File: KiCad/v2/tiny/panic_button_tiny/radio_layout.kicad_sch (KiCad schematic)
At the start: 1 part

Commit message: [UPDATE] some of the pcb design and layout
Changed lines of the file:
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@@
 		(pin "1"
+		)
+		(pin "2"
 		)
 		(instances

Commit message: [UPDATE] some connections in the circuit
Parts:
- added C3: 1.2pF, Capacitor_SMD:C_01005_0402Metric_Pad0.57x0.30mm_HandSolder, symbol PCM_Elektuur:C
- added L1: 4.7nH, Capacitor_SMD:C_0402_1005Metric_Pad0.74x0.62mm_HandSolder, symbol PCM_Elektuur:L
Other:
- moved on the sheet: E1
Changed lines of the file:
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@@
+	)
+	(symbol
+		(lib_id "PCM_Elektuur:L")
+		(at 60.96 31.75 0)
+		(unit 1)
+		(body_style 1)
+		(exclude_from_sim no)
+		(in_bom yes)
+		(on_board yes)
+		(in_pos_files yes)
+		(dnp no)
+		(fields_autoplaced yes)
+		(property "Reference" "L1"
+			(at 63.5 30.4799 0)
+			(show_name no)
+			(do_not_autoplace no)
+			(effects
+				(font
+					(size 1.27 1.27)
+				)
+				(justify left)
+			)
+		)
+		(property "Value" "4.7nH"
+			(at 63.5 33.0199 0)
+			(show_name no)
+			(do_not_autoplace no)
+			(effects
+				(font
+					(size 1.27 1.27)
+				)
+				(justify left)
+			)
+		)
+		(property "Footprint" "Capacitor_SMD:C_0402_1005Metric_Pad0.74x0.62mm_HandSolder"
+			(at 60.96 31.75 0)
+			(hide yes)
+			(show_name no)
+			(do_not_autoplace no)
+			(effects
+				(font
+					(size 1.27 1.27)
+				)
+			)
+		)
+		(property "Datasheet" ""
+			(at 60.96 31.75 0)
+			(hide yes)
+			(show_name no)
+			(do_not_autoplace no)
+			(effects
+				(font
+					(size 1.27 1.27)
+				)
+			)
+		)
+		(property "Description" "coil/winding/inductor/choke/reactor"
+			(at 60.96 31.75 0)
+			(hide yes)
+			(show_name no)
+			(do_not_autoplace no)
+			(effects
+				(font
+					(size 1.27 1.27)
+				)
+			)
+		)
+		(property "Indicator" "●"
+			(at 60.833 29.21 0)
+			(hide yes)
+			(show_name no)
+			(do_not_autoplace no)
+			(effects
+				(font
+					(size 0.635 0.635)
+				)
+			)
+		)
+		(property "Rating" "A"
+			(at 59.69 34.925 0)
+			(hide yes)
+			(show_name no)
+			(do_not_autoplace no)
+			(effects
+				(font
+					(size 1.27 1.27)
+				)
+				(justify right)
+			)
+		)
+		(pin "1"
+		)
+		(pin "2"
+		)
+		(instances
+			(project "panic_button_tiny"
+				(path "/c4eb92e9-b42f-4db0-b1d9-0ef70f7ca601/87783f59-2161-40ec-a051-fa9ad8b0290b"
+					(reference "L1")
+					(unit 1)
+				)
+			)
+		)
 	)
 	(symbol
 		(lib_id "2450AT18A0100001E:2450AT18A0100001E")
-		(at 24.13 22.86 0)
+		(at 24.13 24.13 0)
 		(unit 1)
 		(body_style 1)
@@
 		(fields_autoplaced yes)
 		(property "Reference" "E1"
-			(at 27.94 20.1294 0)
+			(at 28.194 19.812 0)
 			(show_name no)
 			(do_not_autoplace no)
@@
 		)
 		(property "Value" "2450AT18A0100001E"
-			(at 27.94 22.6694 0)
+			(at 27.94 23.9394 0)
 			(show_name no)
 			(do_not_autoplace no)
@@
 		)
 		(property "Footprint" "2450AT18A0100001E:XCVR_2450AT18A0100001E"
-			(at 24.13 22.86 0)
+			(at 22.86 51.308 0)
 			(hide yes)
 			(show_name no)
@@
 		)
 		(property "Datasheet" ""
-			(at 24.13 22.86 0)
+			(at 24.13 24.13 0)
 			(hide yes)
 			(show_name no)
@@
 		)
 		(property "Description" "2.4GHz Chip RF Antenna 2.4GHz ~ 2.5GHz 0.5dBi Solder Surface Mount"
-			(at 24.13 22.86 0)
+			(at 17.78 53.594 0)
 			(hide yes)
 			(show_name no)
@@
 		)
 		(property "MF" "Johanson"
-			(at 24.13 22.86 0)
+			(at 20.066 41.656 0)
 			(hide yes)
 			(show_name no)
@@
 		)
 		(property "MAXIMUM_PACKAGE_HEIGHT" "1.40 mm"
-			(at 24.13 22.86 0)
+			(at 23.876 38.862 0)
 			(hide yes)
 			(show_name no)
@@
 		)
 		(property "Package" "None"
-			(at 24.13 22.86 0)
+			(at 21.59 36.83 0)
 			(hide yes)
 			(show_name no)
@@
 		)
 		(property "Price" "None"
-			(at 24.13 22.86 0)
+			(at 26.67 36.83 0)
 			(hide yes)
 			(show_name no)
@@
 		)
 		(property "Check_prices" "https://www.snapeda.com/parts/2450AT18A0100001E/Johanson/view-part/?ref=eda"
-			(at 24.13 22.86 0)
+			(at 17.272 56.388 0)
 			(hide yes)
 			(show_name no)
@@
 		)
 		(property "STANDARD" "Manufacturer recommendations"
-			(at 24.13 22.86 0)
+			(at 24.638 48.26 0)
 			(hide yes)
 			(show_name no)
@@
 		)
 		(property "PARTREV" "4.0"
-			(at 24.13 22.86 0)
+			(at 24.13 35.306 0)
 			(hide yes)
 			(show_name no)
@@
 		)
 		(property "SnapEDA_Link" "https://www.snapeda.com/parts/2450AT18A0100001E/Johanson/view-part/?ref=snap"
-			(at 24.13 22.86 0)
+			(at 17.526 58.674 0)
 			(hide yes)
 			(show_name no)
@@
 		)
 		(property "MP" "2450AT18A0100001E"
-			(at 24.13 22.86 0)
+			(at 25.908 45.974 0)
 			(hide yes)
 			(show_name no)
@@
 		)
 		(property "Availability" "In Stock"
-			(at 24.13 22.86 0)
+			(at 28.702 41.656 0)
 			(hide yes)
 			(show_name no)
@@
 		)
 		(property "MANUFACTURER" "Johanson Technology"
-			(at 24.13 22.86 0)
+			(at 24.892 43.688 0)
 			(hide yes)
 			(show_name no)
@@
 					(unit 1)
 				)
+			)
+		)
+	)
+	(symbol
+		(lib_id "PCM_Elektuur:C")
+		(at 76.2 31.75 0)
+		(unit 1)
+		(body_style 1)
+		(exclude_from_sim no)
+		(in_bom yes)
+		(on_board yes)
+		(in_pos_files yes)
+		(dnp no)
+		(fields_autoplaced yes)
+		(property "Reference" "C3"
+			(at 80.01 30.4799 0)
+			(show_name no)
+			(do_not_autoplace no)
+			(effects
+				(font
+					(size 1.27 1.27)
+				)
+				(justify left)
+			)
+		)
+		(property "Value" "1.2pF"
+			(at 80.01 33.0199 0)
+			(show_name no)
+			(do_not_autoplace no)
+			(effects
+				(font
+					(size 1.27 1.27)
+				)
+				(justify left)
+			)
+		)
+		(property "Footprint" "Capacitor_SMD:C_01005_0402Metric_Pad0.57x0.30mm_HandSolder"
+			(at 76.2 31.75 0)
+			(hide yes)
+			(show_name no)
+			(do_not_autoplace no)
+			(effects
+				(font
+					(size 1.27 1.27)
+				)
+			)
+		)
+		(property "Datasheet" ""
+			(at 76.2 31.75 0)
+			(hide yes)
+			(show_name no)
+			(do_not_autoplace no)
+			(effects
+				(font
+					(size 1.27 1.27)
+				)
+			)
+		)
+		(property "Description" "capacitor, non-polarized/bipolar"
+			(at 76.2 31.75 0)
+			(hide yes)
+			(show_name no)
+			(do_not_autoplace no)
+			(effects
+				(font
+					(size 1.27 1.27)
+				)
+			)
+		)
+		(property "Indicator" "+"
+			(at 74.93 28.575 0)
+			(hide yes)
+			(show_name no)
+			(do_not_autoplace no)
+			(effects
+				(font
+					(size 1.27 1.27)
+				)
+			)
+		)
+		(property "Rating" "V"
+			(at 75.565 34.925 0)
+			(hide yes)
+			(show_name no)
+			(do_not_autoplace no)
+			(effects
+				(font
+					(size 1.27 1.27)
+				)
+				(justify right)
+			)
+		)
+		(pin "2"
+		)
+		(pin "1"
+		)
+		(instances
+			(project "panic_button_tiny"
+				(path "/c4eb92e9-b42f-4db0-b1d9-0ef70f7ca601/87783f59-2161-40ec-a051-fa9ad8b0290b"
+					(reference "C3")
+					(unit 1)
+				)

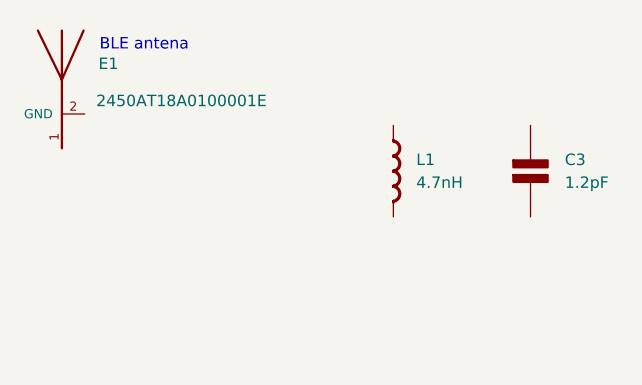
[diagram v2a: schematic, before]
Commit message: [UPDATE] the schematic to reflect the connections of the components
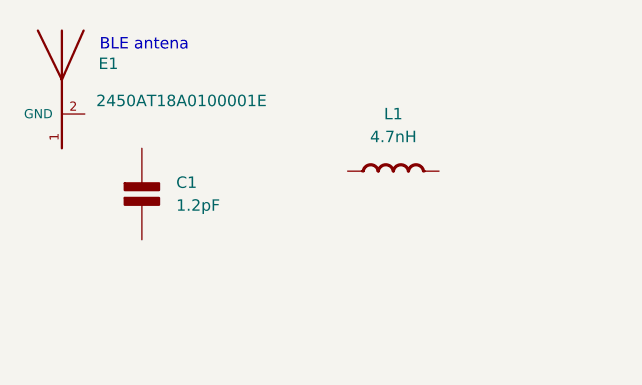
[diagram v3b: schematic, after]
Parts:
- renumbered C3 to C1
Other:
- moved on the sheet: C1, L1
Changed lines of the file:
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@@
 	(symbol
 		(lib_id "PCM_Elektuur:L")
-		(at 60.96 31.75 0)
+		(at 60.96 31.75 90)
 		(unit 1)
 		(body_style 1)
@@
 		(fields_autoplaced yes)
 		(property "Reference" "L1"
-			(at 63.5 30.4799 0)
-			(show_name no)
-			(do_not_autoplace no)
-			(effects
-				(font
-					(size 1.27 1.27)
-				)
-				(justify left)
+			(at 60.96 25.4 90)
+			(show_name no)
+			(do_not_autoplace no)
+			(effects
+				(font
+					(size 1.27 1.27)
+				)
 			)
 		)
 		(property "Value" "4.7nH"
-			(at 63.5 33.0199 0)
-			(show_name no)
-			(do_not_autoplace no)
-			(effects
-				(font
-					(size 1.27 1.27)
-				)
-				(justify left)
+			(at 60.96 27.94 90)
+			(show_name no)
+			(do_not_autoplace no)
+			(effects
+				(font
+					(size 1.27 1.27)
+				)
 			)
 		)
@@
 		)
 		(property "Indicator" "●"
-			(at 60.833 29.21 0)
+			(at 58.42 31.877 0)
 			(hide yes)
 			(show_name no)
@@
 		)
 		(property "Rating" "A"
-			(at 59.69 34.925 0)
+			(at 64.135 33.02 0)
 			(hide yes)
 			(show_name no)
@@
 	(symbol
 		(lib_id "PCM_Elektuur:C")
-		(at 76.2 31.75 0)
+		(at 33.02 34.29 0)
 		(unit 1)
 		(body_style 1)
@@
 		(dnp no)
 		(fields_autoplaced yes)
-		(property "Reference" "C3"
-			(at 80.01 30.4799 0)
+		(property "Reference" "C1"
+			(at 36.83 33.0199 0)
 			(show_name no)
 			(do_not_autoplace no)
@@
 		)
 		(property "Value" "1.2pF"
-			(at 80.01 33.0199 0)
+			(at 36.83 35.5599 0)
 			(show_name no)
 			(do_not_autoplace no)
@@
 		)
 		(property "Footprint" "Capacitor_SMD:C_01005_0402Metric_Pad0.57x0.30mm_HandSolder"
-			(at 76.2 31.75 0)
+			(at 33.02 34.29 0)
 			(hide yes)
 			(show_name no)
@@
 		)
 		(property "Datasheet" ""
-			(at 76.2 31.75 0)
+			(at 33.02 34.29 0)
 			(hide yes)
 			(show_name no)
@@
 		)
 		(property "Description" "capacitor, non-polarized/bipolar"
-			(at 76.2 31.75 0)
+			(at 33.02 34.29 0)
 			(hide yes)
 			(show_name no)
@@
 		)
 		(property "Indicator" "+"
-			(at 74.93 28.575 0)
+			(at 31.75 31.115 0)
 			(hide yes)
 			(show_name no)
@@
 		)
 		(property "Rating" "V"
-			(at 75.565 34.925 0)
+			(at 32.385 37.465 0)
 			(hide yes)
 			(show_name no)
@@
 			(project "panic_button_tiny"
 				(path "/c4eb92e9-b42f-4db0-b1d9-0ef70f7ca601/87783f59-2161-40ec-a051-fa9ad8b0290b"
-					(reference "C3")
+					(reference "C1")
 					(unit 1)
 				)

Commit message: [UPDATE] the schematic wirering
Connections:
- net GND: now reaches L1.1 (+)
- net at L1.2 (-): now also E1.2 (GND)
- net at E1.1: now also C1.1 (+)
- net BLE_ant_in: now reaches C1.2 (-)
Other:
- moved on the sheet: C1, L1
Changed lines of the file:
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@@
+		)
+	)
+	(hierarchical_label "BLE_ant_in"
+		(shape input)
+		(at 24.13 39.37 270)
+		(effects
+			(font
+				(size 1.27 1.27)
+			)
+			(justify right)
 		)
 	)
 	(symbol
 		(lib_id "PCM_Elektuur:L")
-		(at 60.96 31.75 90)
+		(at 31.75 25.4 270)
 		(unit 1)
 		(body_style 1)
@@
 		(in_pos_files yes)
 		(dnp no)
-		(fields_autoplaced yes)
 		(property "Reference" "L1"
-			(at 60.96 25.4 90)
+			(at 32.004 30.734 90)
 			(show_name no)
 			(do_not_autoplace no)
@@
 		)
 		(property "Value" "4.7nH"
-			(at 60.96 27.94 90)
+			(at 32.004 28.194 90)
 			(show_name no)
 			(do_not_autoplace no)
@@
 		)
 		(property "Footprint" "Capacitor_SMD:C_0402_1005Metric_Pad0.74x0.62mm_HandSolder"
-			(at 60.96 31.75 0)
+			(at 31.75 25.4 0)
 			(hide yes)
 			(show_name no)
@@
 		)
 		(property "Datasheet" ""
-			(at 60.96 31.75 0)
+			(at 31.75 25.4 0)
 			(hide yes)
 			(show_name no)
@@
 		)
 		(property "Description" "coil/winding/inductor/choke/reactor"
-			(at 60.96 31.75 0)
+			(at 31.75 25.4 0)
 			(hide yes)
 			(show_name no)
@@
 		)
 		(property "Indicator" "●"
-			(at 58.42 31.877 0)
+			(at 34.29 25.273 0)
 			(hide yes)
 			(show_name no)
@@
 		)
 		(property "Rating" "A"
-			(at 64.135 33.02 0)
+			(at 28.575 24.13 0)
 			(hide yes)
 			(show_name no)
@@
 		(in_pos_files yes)
 		(dnp no)
-		(fields_autoplaced yes)
 		(property "Reference" "E1"
 			(at 28.194 19.812 0)
@@
 		)
 		(property "Value" "2450AT18A0100001E"
-			(at 27.94 23.9394 0)
+			(at 31.242 20.066 0)
 			(show_name no)
 			(do_not_autoplace no)
@@
 	(symbol
 		(lib_id "PCM_Elektuur:C")
-		(at 33.02 34.29 0)
+		(at 24.13 34.29 0)
 		(unit 1)
 		(body_style 1)
@@
 		(fields_autoplaced yes)
 		(property "Reference" "C1"
-			(at 36.83 33.0199 0)
+			(at 27.94 33.0199 0)
 			(show_name no)
 			(do_not_autoplace no)
@@
 		)
 		(property "Value" "1.2pF"
-			(at 36.83 35.5599 0)
+			(at 27.94 35.5599 0)
 			(show_name no)
 			(do_not_autoplace no)
@@
 		)
 		(property "Footprint" "Capacitor_SMD:C_01005_0402Metric_Pad0.57x0.30mm_HandSolder"
-			(at 33.02 34.29 0)
+			(at 24.13 34.29 0)
 			(hide yes)
 			(show_name no)
@@
 		)
 		(property "Datasheet" ""
-			(at 33.02 34.29 0)
+			(at 24.13 34.29 0)
 			(hide yes)
 			(show_name no)
@@
 		)
 		(property "Description" "capacitor, non-polarized/bipolar"
-			(at 33.02 34.29 0)
+			(at 24.13 34.29 0)
 			(hide yes)
 			(show_name no)
@@
 		)
 		(property "Indicator" "+"
-			(at 31.75 31.115 0)
+			(at 22.86 31.115 0)
 			(hide yes)
 			(show_name no)
@@
 		)
 		(property "Rating" "V"
-			(at 32.385 37.465 0)
+			(at 23.495 37.465 0)
 			(hide yes)
 			(show_name no)
@@
 					(unit 1)
 				)
+			)
+		)
+	)
+	(symbol
+		(lib_id "PCM_SparkFun-PowerSymbol:GND")
+		(at 36.83 25.4 0)
+		(unit 1)
+		(body_style 1)
+		(exclude_from_sim no)
+		(in_bom yes)
+		(on_board yes)
+		(in_pos_files yes)
+		(dnp no)
+		(fields_autoplaced yes)
+		(property "Reference" "#PWR073"
+			(at 36.83 31.75 0)
+			(hide yes)
+			(show_name no)
+			(do_not_autoplace no)
+			(effects
+				(font
+					(size 1.27 1.27)
+				)
+			)
+		)
+		(property "Value" "GND"
+			(at 36.83 29.21 0)
+			(show_name no)
+			(do_not_autoplace yes)
+			(effects
+				(font
+					(size 1.27 1.27)
+				)
+			)
+		)
+		(property "Footprint" ""
+			(at 36.83 25.4 0)
+			(hide yes)
+			(show_name no)
+			(do_not_autoplace no)
+			(effects
+				(font
+					(size 1.27 1.27)
+				)
+			)
+		)
+		(property "Datasheet" ""
+			(at 36.83 25.4 0)
+			(hide yes)
+			(show_name no)
+			(do_not_autoplace no)
+			(effects
+				(font
+					(size 1.27 1.27)
+				)
+			)
+		)
+		(property "Description" "Power symbol creates a global label with name \"GND\" , ground"
+			(at 36.83 34.29 0)
+			(hide yes)
+			(show_name no)
+			(do_not_autoplace no)
+			(effects
+				(font
+					(size 1.27 1.27)
+				)
+			)
+		)
+		(pin "1"
+		)
+		(instances
+			(project "panic_button_tiny"
+				(path "/c4eb92e9-b42f-4db0-b1d9-0ef70f7ca601/87783f59-2161-40ec-a051-fa9ad8b0290b"
+					(reference "#PWR073")
+					(unit 1)
+				)
